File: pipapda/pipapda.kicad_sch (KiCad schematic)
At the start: 0 parts

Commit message: add switches to schematic
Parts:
- added D1, D10, D11, D12, D13, D14, D15, D16, D17, D18, D19, D2, D20, D21, D22, D23, D24, D26, D27, D28, D29, D3, D30, D31, D32, D33, D34, D36, D37, D38, D39, D4, D41, D42, D43, D44, D45, D46, D47, D48, D49, D5, D50, D51, D52, D53, D54, D55, D56, D57, D58, D59, D6, D60, D7, D8, D9: 1N5819WS, PCM_JLCPCB:D_SOD-323, symbol PCM_JLCPCB-Diodes:Schottky,1N5819WS
- added S1, S10, S11, S12, S13, S14, S15, S16, S17, S18, S19, S2, S20, S21, S22, S23, S24, S26, S27, S28, S29, S3, S30, S31, S32, S33, S34, S36, S37, S38, S39, S4, S41, S42, S43, S44, S45, S46, S47, S48, S49, S5, S50, S51, S52, S53, S54, S55, S56, S57, S58, S59, S6, S60, S7, S8, S9: Tactile Button, 160gf, PCM_JLCPCB:SW-SMD_4P-L5.1-W5.1-P3.70-LS6.5-TL-2, symbol PCM_JLCPCB-Connectors_Buttons:Tactile Button, 160gf, 12V, 50mA, 5.1mm
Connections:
- new net: D16.2, S16.4 (D)
- new net: D39.2, S39.4 (D)
- new net: D28.2, S28.4 (D)
- new net: D7.2, S7.4 (D)
- new net: D6.2, S6.4 (D)
- new net: D23.2, S23.4 (D)
- new net: D5.2, S5.4 (D)
- new net: D41.2, S41.4 (D)
- new net: D26.2, S26.4 (D)
- new net: D56.2, S56.4 (D)
- new net: D36.2, S36.4 (D)
- new net: D13.2, S13.4 (D)
- new net: D11.2, S11.4 (D)
- new net: D3.2, S3.4 (D)
- new net: D17.2, S17.4 (D)
- new net: D48.2, S48.4 (D)
- new net: D27.2, S27.4 (D)
- new net: D34.2, S34.4 (D)
- new net: D60.2, S60.4 (D)
- new net: D15.2, S15.4 (D)
- new net: D46.2, S46.4 (D)
- new net: D32.2, S32.4 (D)
- new net: D18.2, S18.4 (D)
- new net: D52.2, S52.4 (D)
- new net: D45.2, S45.4 (D)
- new net: D57.2, S57.4 (D)
- new net: D9.2, S9.4 (D)
- new net: D33.2, S33.4 (D)
- new net: D43.2, S43.4 (D)
- new net: D51.2, S51.4 (D)
- new net: D21.2, S21.4 (D)
- new net: D55.2, S55.4 (D)
- new net: D4.2, S4.4 (D)
- new net: D37.2, S37.4 (D)
- new net: D47.2, S47.4 (D)
- new net: D14.2, S14.4 (D)
- new net: D49.2, S49.4 (D)
- new net: D2.2, S2.4 (D)
- new net: D10.2, S10.4 (D)
- new net: D1.2, S1.4 (D)
- new net: D24.2, S24.4 (D)
- new net: D59.2, S59.4 (D)
- new net: D20.2, S20.4 (D)
- new net: D53.2, S53.4 (D)
- new net: D29.2, S29.4 (D)
- new net: D42.2, S42.4 (D)
- new net: D58.2, S58.4 (D)
- new net: D19.2, S19.4 (D)
- new net: D44.2, S44.4 (D)
- new net: D22.2, S22.4 (D)
- new net: D31.2, S31.4 (D)
- new net: D54.2, S54.4 (D)
- new net: D8.2, S8.4 (D)
- new net: D50.2, S50.4 (D)
- new net: D38.2, S38.4 (D)
- new net: D30.2, S30.4 (D)
- new net: D12.2, S12.4 (D)
- new net Col0: S1.1 (A), S3.1 (A), S5.1 (A), S7.1 (A), S9.1 (A)
- new net Col1: S10.1 (A), S2.1 (A), S4.1 (A), S6.1 (A), S8.1 (A)
- new net Col10: S51.1 (A), S52.1 (A), S53.1 (A), S54.1 (A), S55.1 (A)
- new net Col11: S56.1 (A), S57.1 (A), S58.1 (A), S59.1 (A), S60.1 (A)
- new net Col2: S11.1 (A), S12.1 (A), S13.1 (A), S14.1 (A), S15.1 (A)
- new net Col3: S16.1 (A), S17.1 (A), S18.1 (A), S19.1 (A), S20.1 (A)
- new net Col4: S21.1 (A), S22.1 (A), S23.1 (A), S24.1 (A)
- new net Col5: S26.1 (A), S27.1 (A), S28.1 (A), S29.1 (A), S30.1 (A)
- new net Col6: S31.1 (A), S32.1 (A), S33.1 (A), S34.1 (A)
- new net Col7: S36.1 (A), S37.1 (A), S38.1 (A), S39.1 (A)
- new net Col8: S41.1 (A), S42.1 (A), S43.1 (A), S44.1 (A), S45.1 (A)
- new net Col9: S46.1 (A), S47.1 (A), S48.1 (A), S49.1 (A), S50.1 (A)
- new net Row0: D1.1, D11.1, D16.1, D2.1, D21.1, D26.1, D31.1, D36.1, D41.1, D46.1, D51.1, D56.1
- new net Row1: D12.1, D17.1, D22.1, D27.1, D3.1, D32.1, D37.1, D4.1, D42.1, D47.1, D52.1, D57.1
- new net Row2: D13.1, D18.1, D23.1, D28.1, D33.1, D38.1, D43.1, D48.1, D5.1, D53.1, D58.1, D6.1
- new net Row3: D14.1, D19.1, D24.1, D29.1, D34.1, D39.1, D44.1, D49.1, D54.1, D59.1, D7.1, D8.1
- new net Row4: D10.1, D15.1, D20.1, D30.1, D45.1, D50.1, D55.1, D60.1, D9.1

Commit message: add internal parts to mockup
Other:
- note added: "Keyboard"
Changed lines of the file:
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@@
 	(generator "eeschema")
 	(generator_version "10.0")
-	(paper "A4")
+	(paper "A3")
+	(rectangle
+		(start 13.97 17.78)
+		(end 210.82 151.13)
+		(stroke
+			(width 0)
+			(type default)
+		)
+		(fill
+			(type none)
+		)
+	)
+	(text "Keyboard\n"
+		(exclude_from_sim no)
+		(at 204.724 150.368 0)
+		(effects
+			(font
+				(size 1.27 1.27)
+			)
+		)
+	)
 	(junction
 		(at 77.47 96.52)

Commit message: work on PCB
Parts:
- added C1: C, symbol Device:C
- added U1: ZX-FPC-FWX0.5PH218, easyeda2kicad:FPC-SMD_18P-P0.50_MEGASTAR_ZX-FPC-FWX0.5PH218, symbol easyeda2kicad:ZX-FPC-FWX0.5PH218
- added U2: STM32F103RGTx, Package_QFP:LQFP-64_10x10mm_P0.5mm, symbol MCU_ST_STM32F1:STM32F103RGTx
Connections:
- new net: U2.18 (VSS), U2.31 (VSS), U2.47 (VSS), U2.63 (VSS)

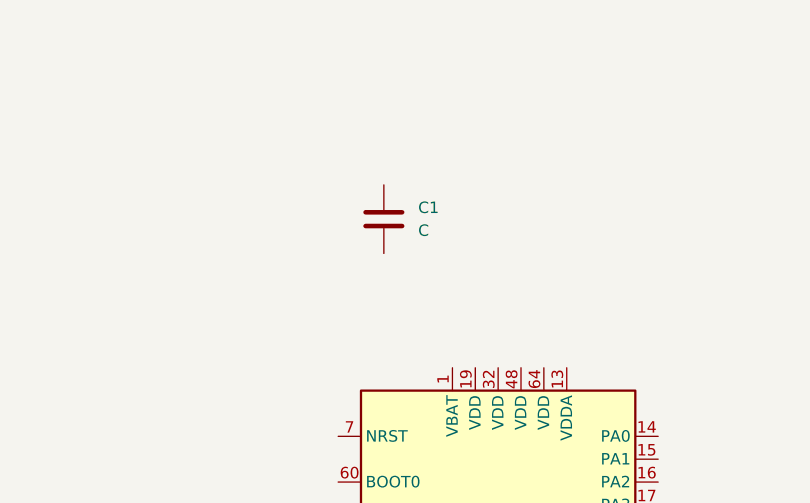
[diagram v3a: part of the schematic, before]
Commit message: migrate all parts to easyeda2kicad footprints
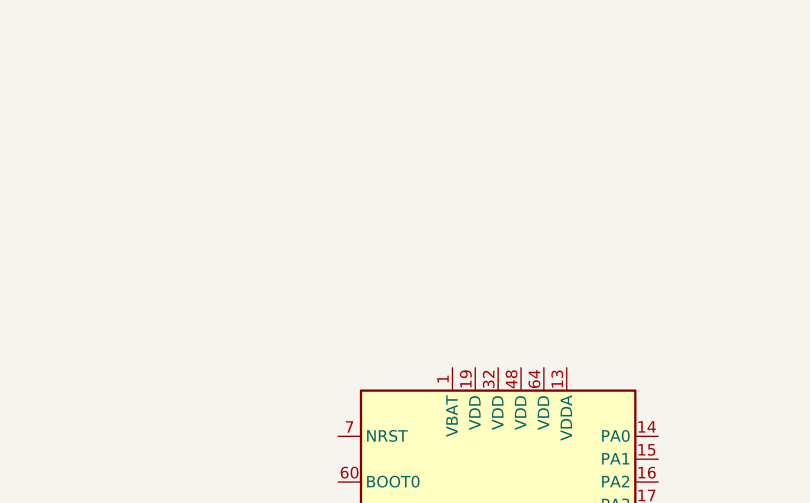
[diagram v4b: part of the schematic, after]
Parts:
- removed C1: C, symbol Device:C
- D1, D10, D11, D12, D13, D14, D15, D16, D17, D18, D19, D2, D20, D21, D22, D23, D24, D26, D27, D28, D29, D3, D30, D31, D32, D33, D34, D36, D37, D38, D39, D4, D41, D42, D43, D44, D45, D46, D47, D48, D49, D5, D50, D51, D52, D53, D54, D55, D56, D57, D58, D59, D6, D60, D7, D8, D9: footprint PCM_JLCPCB:D_SOD-323 -> easyeda2kicad:SOD-323_L1.8-W1.3-LS2.5-RD
- S1, S10, S11, S12, S13, S14, S15, S16, S17, S18, S19, S2, S20, S21, S22, S23, S24, S26, S27, S28, S29, S3, S30, S31, S32, S33, S34, S36, S37, S38, S39, S4, S41, S42, S43, S44, S45, S46, S47, S48, S49, S5, S50, S51, S52, S53, S54, S55, S56, S57, S58, S59, S6, S60, S7, S8, S9: footprint PCM_JLCPCB:SW-SMD_4P-L5.1-W5.1-P3.70-LS6.5-TL-2 -> easyeda2kicad:SW-SMD_4P-L5.1-W5.1-P3.70-LS6.5-TL_H1.5

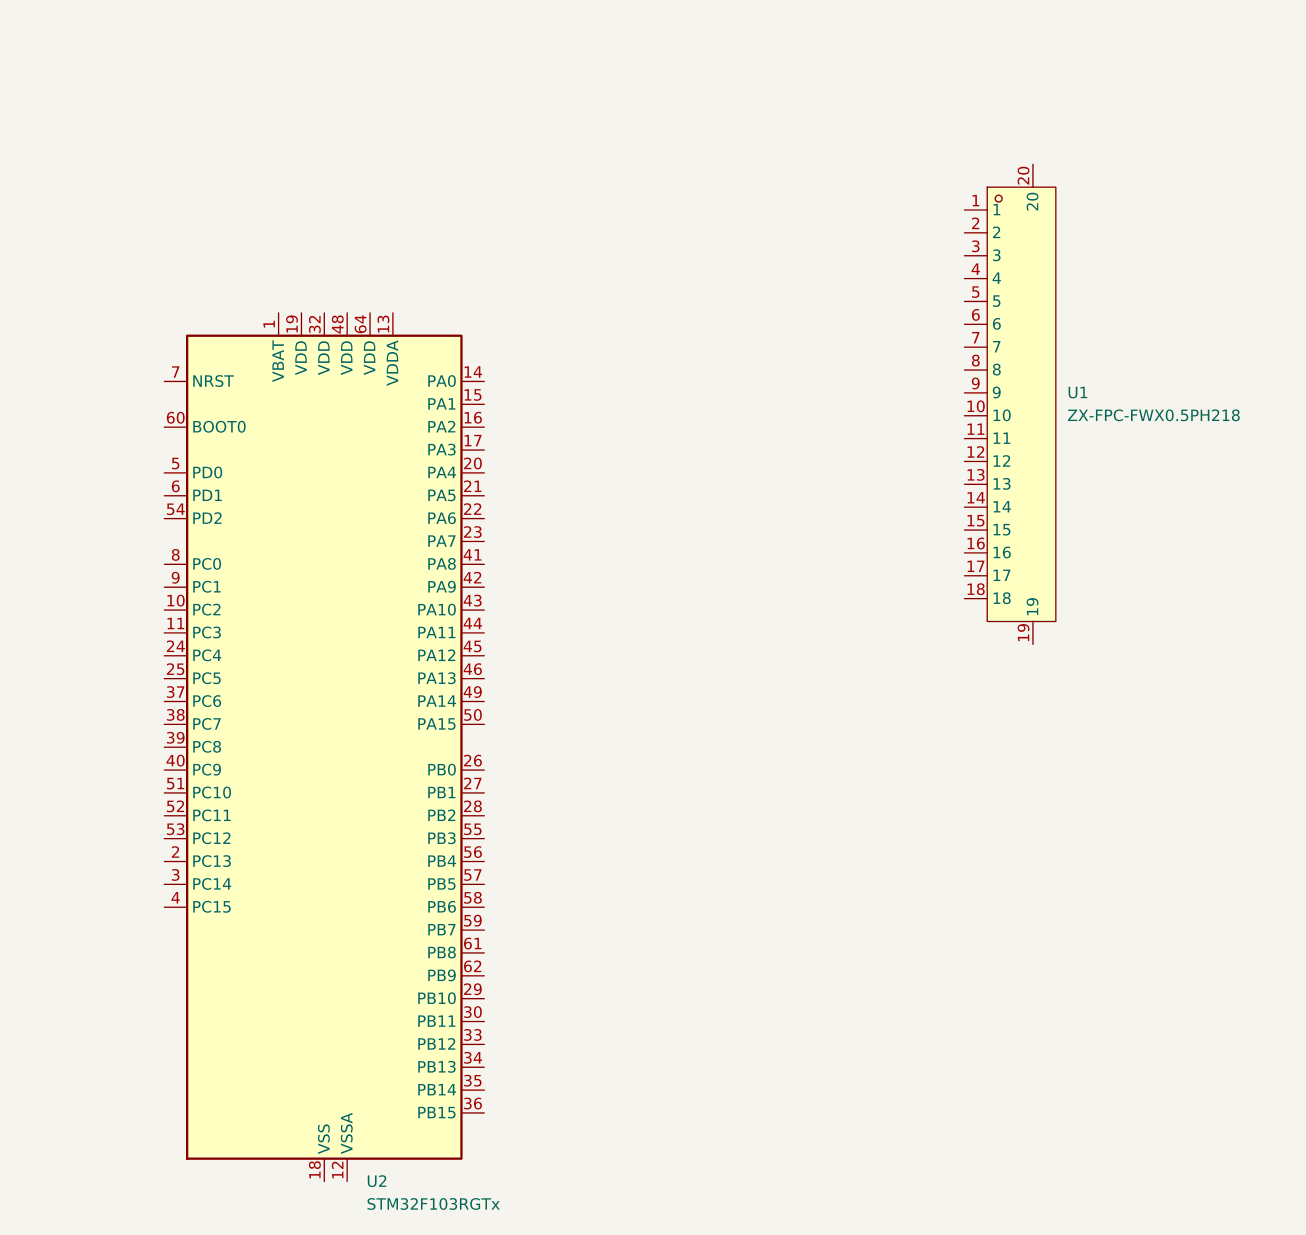
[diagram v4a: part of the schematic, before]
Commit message: replace connector with proper one
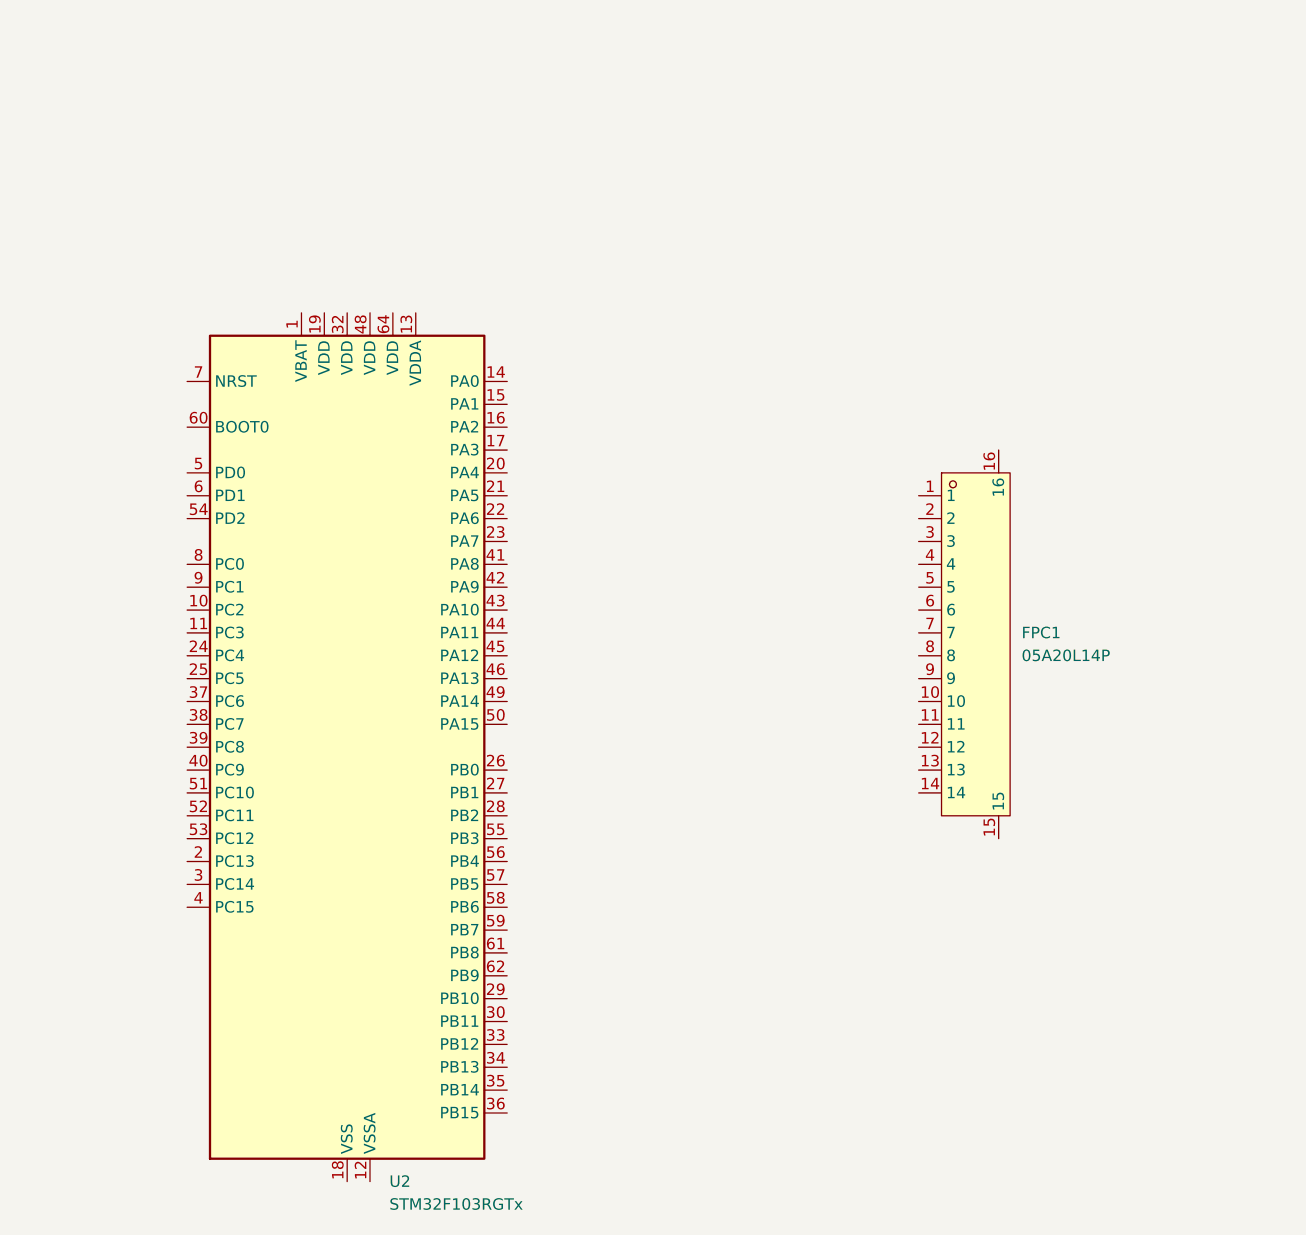
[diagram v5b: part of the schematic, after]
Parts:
- removed U1: ZX-FPC-FWX0.5PH218, easyeda2kicad:FPC-SMD_18P-P0.50_MEGASTAR_ZX-FPC-FWX0.5PH218, symbol easyeda2kicad:ZX-FPC-FWX0.5PH218
- added FPC1: 05A20L14P, easyeda2kicad:CONN-SMD_05A20L14P, symbol easyeda2kicad:05A20L14P
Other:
- moved on the sheet: U2
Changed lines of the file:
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@@
 	)
 	(symbol
-		(lib_id "easyeda2kicad:ZX-FPC-FWX0.5PH218")
-		(at 353.06 64.77 0)
-		(unit 1)
-		(body_style 1)
-		(exclude_from_sim no)
-		(in_bom yes)
-		(on_board yes)
-		(in_pos_files yes)
-		(dnp no)
-		(fields_autoplaced yes)
-		(property "Reference" "U1"
-			(at 359.41 63.4999 0)
-			(show_name no)
-			(do_not_autoplace no)
-			(effects
-				(font
-					(size 1.27 1.27)
-				)
-				(justify left)
-			)
-		)
-		(property "Value" "ZX-FPC-FWX0.5PH218"
-			(at 359.41 66.0399 0)
-			(show_name no)
-			(do_not_autoplace no)
-			(effects
-				(font
-					(size 1.27 1.27)
-				)
-				(justify left)
-			)
-		)
-		(property "Footprint" "easyeda2kicad:FPC-SMD_18P-P0.50_MEGASTAR_ZX-FPC-FWX0.5PH218"
-			(at 353.06 99.06 0)
-			(hide yes)
-			(show_name no)
-			(do_not_autoplace no)
-			(effects
-				(font
-					(size 1.27 1.27)
-				)
-			)
-		)
-		(property "Datasheet" "https://www.lcsc.com/datasheet/C7419868.pdf"
-			(at 353.06 101.6 0)
-			(hide yes)
-			(show_name no)
-			(do_not_autoplace no)
-			(effects
-				(font
-					(size 1.27 1.27)
-				)
-			)
-		)
-		(property "Description" ""
-			(at 353.06 64.77 0)
-			(hide yes)
-			(show_name no)
-			(do_not_autoplace no)
-			(effects
-				(font
-					(size 1.27 1.27)
-				)
-			)
-		)
-		(property "Manufacturer" "Megastar(兆星)"
-			(at 353.06 104.14 0)
-			(hide yes)
-			(show_name no)
-			(do_not_autoplace no)
-			(effects
-				(font
-					(size 1.27 1.27)
-				)
-			)
-		)
-		(property "MPN" "ZX-FPC-FWX0.5PH218"
-			(at 353.06 106.68 0)
-			(hide yes)
-			(show_name no)
-			(do_not_autoplace no)
-			(effects
-				(font
-					(size 1.27 1.27)
-				)
-			)
-		)
-		(property "LCSC Part" "C7419868"
-			(at 353.06 109.22 0)
-			(hide yes)
-			(show_name no)
-			(do_not_autoplace no)
-			(effects
-				(font
-					(size 1.27 1.27)
-				)
-			)
-		)
-		(pin "20"
-		)
-		(pin "19"
-		)
-		(pin "15"
-		)
-		(pin "18"
-		)
-		(pin "17"
-		)
-		(pin "16"
-		)
-		(pin "14"
-		)
-		(pin "13"
-		)
-		(pin "12"
-		)
-		(pin "11"
-		)
-		(pin "10"
-		)
-		(pin "9"
-		)
-		(pin "8"
-		)
-		(pin "7"
-		)
-		(pin "6"
-		)
-		(pin "5"
-		)
-		(pin "4"
-		)
-		(pin "3"
-		)
-		(pin "2"
-		)
-		(pin "1"
-		)
-		(instances
-			(project "pipapda"
-				(path "/d1aa8f6c-1644-4347-b86d-2b771500f753"
-					(reference "U1")
-					(unit 1)
-				)
-			)
-		)
-	)
-	(symbol
 		(lib_id "PCM_JLCPCB-Connectors_Buttons:Tactile Button, 160gf, 12V, 50mA, 5.1mm")
 		(at 44.45 34.29 0)
@@
 	)
 	(symbol
+		(lib_id "easyeda2kicad:05A20L14P")
+		(at 347.98 91.44 0)
+		(unit 1)
+		(body_style 1)
+		(exclude_from_sim no)
+		(in_bom yes)
+		(on_board yes)
+		(in_pos_files yes)
+		(dnp no)
+		(fields_autoplaced yes)
+		(property "Reference" "FPC1"
+			(at 354.33 90.1699 0)
+			(show_name no)
+			(do_not_autoplace no)
+			(effects
+				(font
+					(size 1.27 1.27)
+				)
+				(justify left)
+			)
+		)
+		(property "Value" "05A20L14P"
+			(at 354.33 92.7099 0)
+			(show_name no)
+			(do_not_autoplace no)
+			(effects
+				(font
+					(size 1.27 1.27)
+				)
+				(justify left)
+			)
+		)
+		(property "Footprint" "easyeda2kicad:CONN-SMD_05A20L14P"
+			(at 347.98 120.65 0)
+			(hide yes)
+			(show_name no)
+			(do_not_autoplace no)
+			(effects
+				(font
+					(size 1.27 1.27)
+				)
+			)
+		)
+		(property "Datasheet" "https://www.lcsc.com/datasheet/C22435642.pdf"
+			(at 347.98 123.19 0)
+			(hide yes)
+			(show_name no)
+			(do_not_autoplace no)
+			(effects
+				(font
+					(size 1.27 1.27)
+				)
+			)
+		)
+		(property "Description" ""
+			(at 347.98 91.44 0)
+			(hide yes)
+			(show_name no)
+			(do_not_autoplace no)
+			(effects
+				(font
+					(size 1.27 1.27)
+				)
+			)
+		)
+		(property "Manufacturer" "HanElectricity(瀚源)"
+			(at 347.98 125.73 0)
+			(hide yes)
+			(show_name no)
+			(do_not_autoplace no)
+			(effects
+				(font
+					(size 1.27 1.27)
+				)
+			)
+		)
+		(property "MPN" "05A20L14P"
+			(at 347.98 128.27 0)
+			(hide yes)
+			(show_name no)
+			(do_not_autoplace no)
+			(effects
+				(font
+					(size 1.27 1.27)
+				)
+			)
+		)
+		(property "LCSC Part" "C22435642"
+			(at 347.98 130.81 0)
+			(hide yes)
+			(show_name no)
+			(do_not_autoplace no)
+			(effects
+				(font
+					(size 1.27 1.27)
+				)
+			)
+		)
+		(pin "7"
+		)
+		(pin "9"
+		)
+		(pin "1"
+		)
+		(pin "2"
+		)
+		(pin "3"
+		)
+		(pin "4"
+		)
+		(pin "5"
+		)
+		(pin "6"
+		)
+		(pin "8"
+		)
+		(pin "10"
+		)
+		(pin "11"
+		)
+		(pin "12"
+		)
+		(pin "14"
+		)
+		(pin "15"
+		)
+		(pin "16"
+		)
+		(pin "13"
+		)
+		(instances
+			(project "pipapda"
+				(path "/d1aa8f6c-1644-4347-b86d-2b771500f753"
+					(reference "FPC1")
+					(unit 1)
+				)
+			)
+		)
+	)
+	(symbol
 		(lib_id "PCM_JLCPCB-Connectors_Buttons:Tactile Button, 160gf, 12V, 50mA, 5.1mm")
 		(at 156.21 80.01 0)
@@
 	(symbol
 		(lib_id "MCU_ST_STM32F1:STM32F103RGTx")
-		(at 276.86 102.87 0)
+		(at 279.4 102.87 0)
 		(unit 1)
 		(body_style 1)
@@
 		(fields_autoplaced yes)
 		(property "Reference" "U2"
-			(at 281.5433 151.13 0)
+			(at 284.0833 151.13 0)
 			(show_name no)
 			(do_not_autoplace no)
@@
 		)
 		(property "Value" "STM32F103RGTx"
-			(at 281.5433 153.67 0)
+			(at 284.0833 153.67 0)
 			(show_name no)
 			(do_not_autoplace no)
@@
 		)
 		(property "Footprint" "Package_QFP:LQFP-64_10x10mm_P0.5mm"
-			(at 261.62 148.59 0)
+			(at 264.16 148.59 0)
 			(hide yes)
 			(show_name no)
@@
 		)
 		(property "Datasheet" "https://www.st.com/resource/en/datasheet/stm32f103rg.pdf"
-			(at 276.86 102.87 0)
+			(at 279.4 102.87 0)
 			(hide yes)
 			(show_name no)
@@
 		)
 		(property "Description" "STMicroelectronics Arm Cortex-M3 MCU, 1024KB flash, 96KB RAM, 72 MHz, 2.0-3.6V, 51 GPIO, LQFP64"
-			(at 276.86 102.87 0)
+			(at 279.4 102.87 0)
 			(hide yes)
 			(show_name no)
